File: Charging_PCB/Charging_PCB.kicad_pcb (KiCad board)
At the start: 2 copper layers, 8 parts, among them K3 BMS_Relay, K4 IMD_Relay, Q1 PMOS, Q2 PMOS

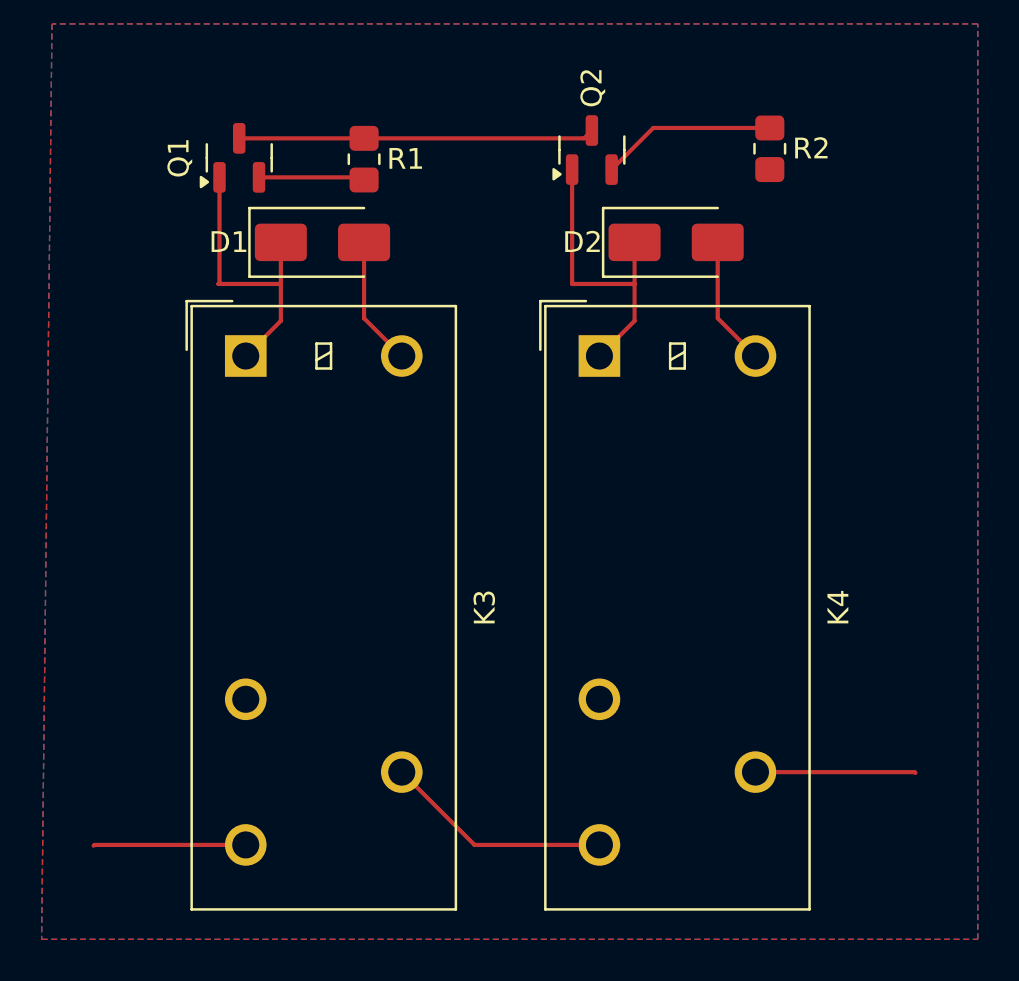
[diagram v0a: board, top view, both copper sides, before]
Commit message: unfinished connector addition to schematic
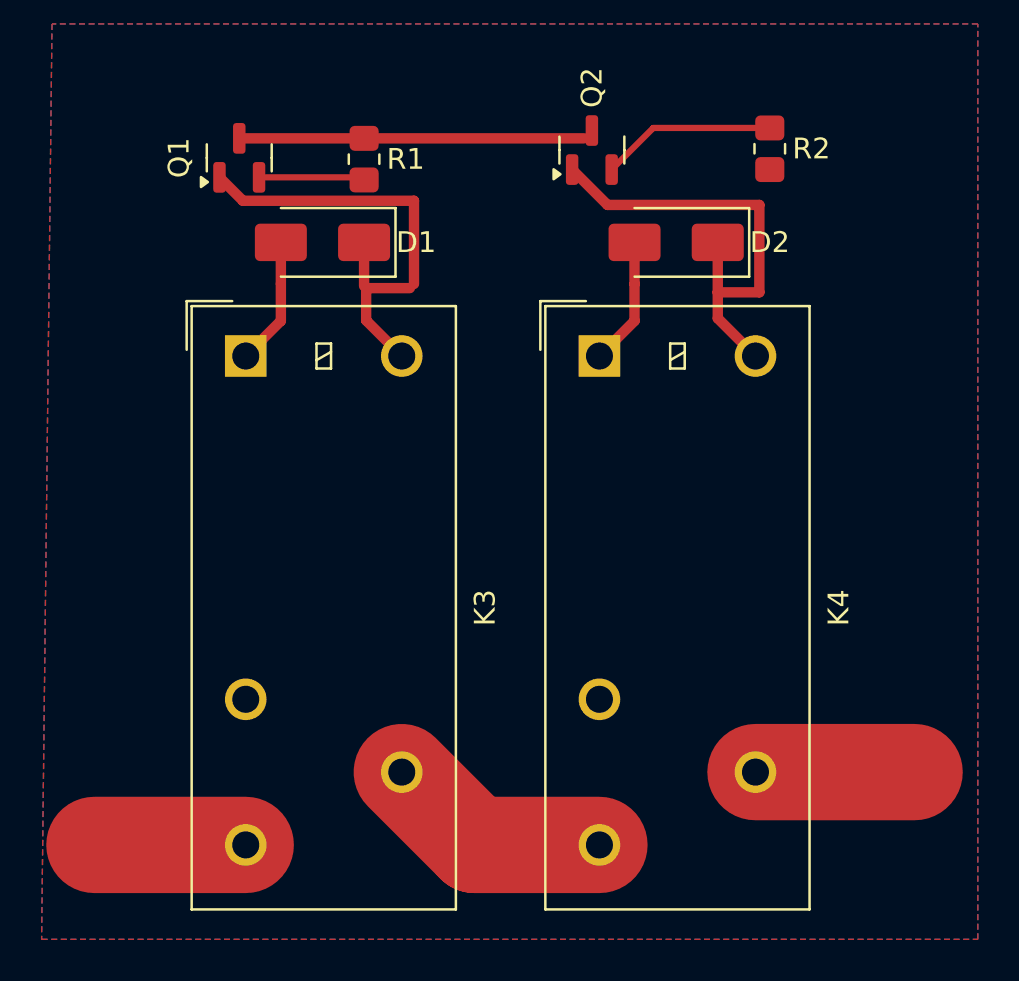
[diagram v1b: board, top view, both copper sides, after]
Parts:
- turned D1 to 180 degrees
- turned D2 to 180 degrees
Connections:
- D1 pad 2: GND -> /+12_Relay
- D2 pad 2: GND -> /+12_Relay
- K3 pad 11: Net-(K3-Pad11) -> /+12_Relay
- K3 pad A1: GND -> /+12_Relay
- K4 pad 11: Net-(K4-Pad11) -> /+12_Relay
- K4 pad 14: Net-(K3-Pad11) -> /+12_Relay
- K4 pad A1: GND -> /+12_Relay
- R2 pad 2: GND -> Net-(K3-Pad11)
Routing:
- net /+12_Relay: track 7.33 -> 38.3 mm
- net GND: track 12.4 -> 0.00 mm
- net Net-(K3-Pad11): track 10.9 -> 0.00 mm
- net Net-(D1-K): track 14.3 -> 22.4 mm
- net Net-(K4-Pad11): track 7.70 -> 0.00 mm
- net Net-(D2-K): track 14.7 -> 22.1 mm

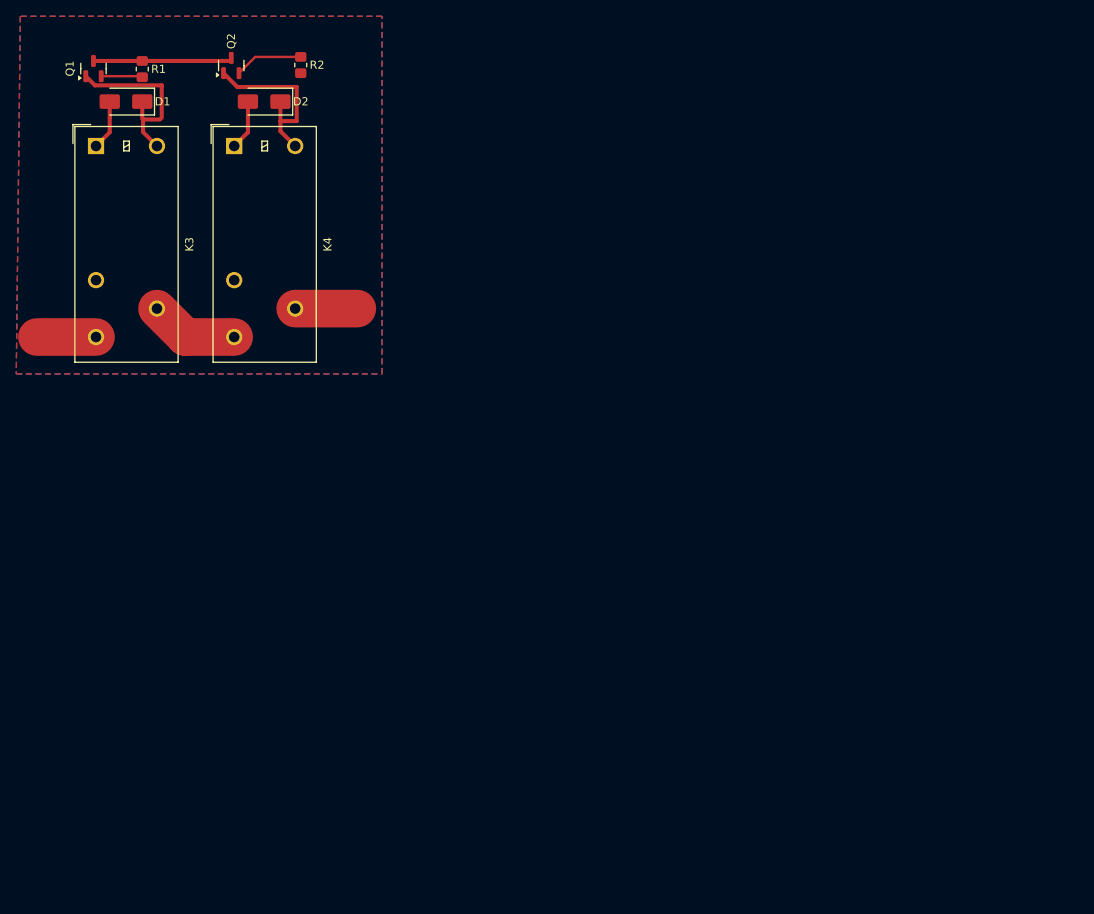
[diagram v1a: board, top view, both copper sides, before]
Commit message: added connectors, relay traces, mounting holes, labels
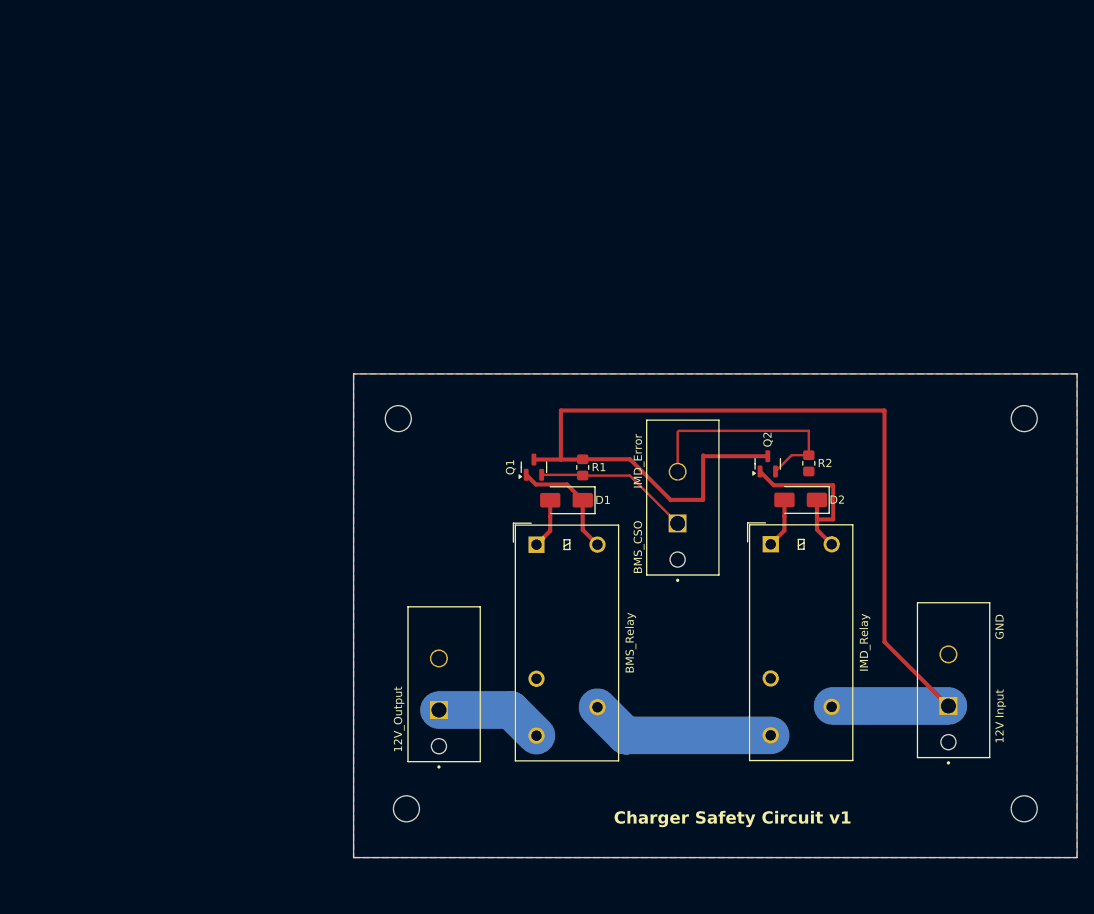
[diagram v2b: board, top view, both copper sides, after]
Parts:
- added 12V Input              GND: 12V Input, 641964-1:TE_641964-1, F.Cu at (179.7, 114.8)
- added 12V_Output: Relay Output, 641964-1:TE_641964-1, F.Cu at (117.0, 115.3)
- added BMS_CSO         IMD_Error: Signal Inputs, 641964-1:TE_641964-1, F.Cu at (146.4, 92.4)
- added H101: MountingHole, MountingHole:MountingHole_3.2mm_M3, F.Cu at (189.0, 79.5)
- added H102: MountingHole, MountingHole:MountingHole_3.2mm_M3, F.Cu at (112.0, 79.5)
- added H103: MountingHole, MountingHole:MountingHole_3.2mm_M3, F.Cu at (189.0, 127.5)
- added H104: MountingHole, MountingHole:MountingHole_3.2mm_M3, F.Cu at (113.0, 127.5)
- moved D2 82.2 mm to (161.5, 89.5)
- moved IMD_Relay 82.2 mm to (157.8, 95.0)
- moved Q2 82.2 mm to (157.4, 85.1)
- moved R2 79.4 mm to (162.5, 85.0)
- moved BMS_Relay 73.1 mm to (129.0, 95.0)
- moved D1 73.1 mm to (132.7, 89.5)
- moved Q1 73.1 mm to (128.7, 85.5)
- moved R1 73.1 mm to (134.7, 85.5)
- renumbered K3 to BMS_Relay, K4 to IMD_Relay
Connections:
- net /CSO renamed /BMS_CSO
- net /IMD_error renamed /IMD_Error
- BMS_Relay pad 11: /+12_Relay -> Net-(K3-Pad11)
- BMS_Relay pad A1: /+12_Relay -> GND
- D1 pad 2: /+12_Relay -> GND
- D2 pad 2: /+12_Relay -> GND
- IMD_Relay pad 11: /+12_Relay -> +12V
- IMD_Relay pad 14: /+12_Relay -> Net-(K3-Pad11)
- IMD_Relay pad A1: /+12_Relay -> GND
- R2 pad 2: Net-(K3-Pad11) -> GND
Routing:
- net +12V: track 17.1 -> 136.3 mm
- net /+12_Relay: track 38.3 -> 13.3 mm
- net Net-(K3-Pad11): track 0.00 -> 22.8 mm
- net /IMD_Error: track 8.43 -> 29.0 mm
- net /BMS_CSO: track 5.10 -> 19.2 mm
- net GND: track 0.00 -> 12.3 mm
- net Net-(D1-K): track 22.4 -> 14.5 mm
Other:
- board outline added: 89 x 59.5 mm
- board text added: "Charger Safety Circuit v1"

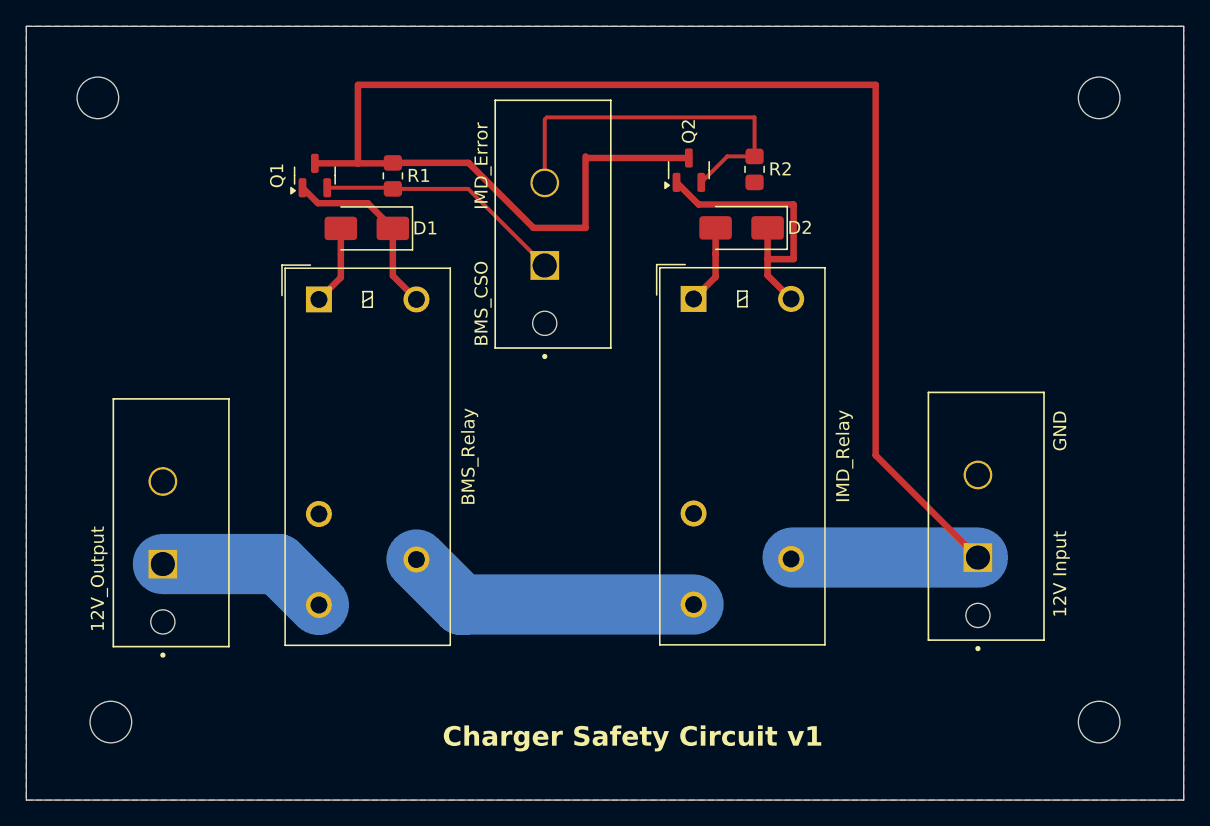
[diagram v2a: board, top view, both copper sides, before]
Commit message: Fillet edges, shrunk relay traces, fixed labels for vinh
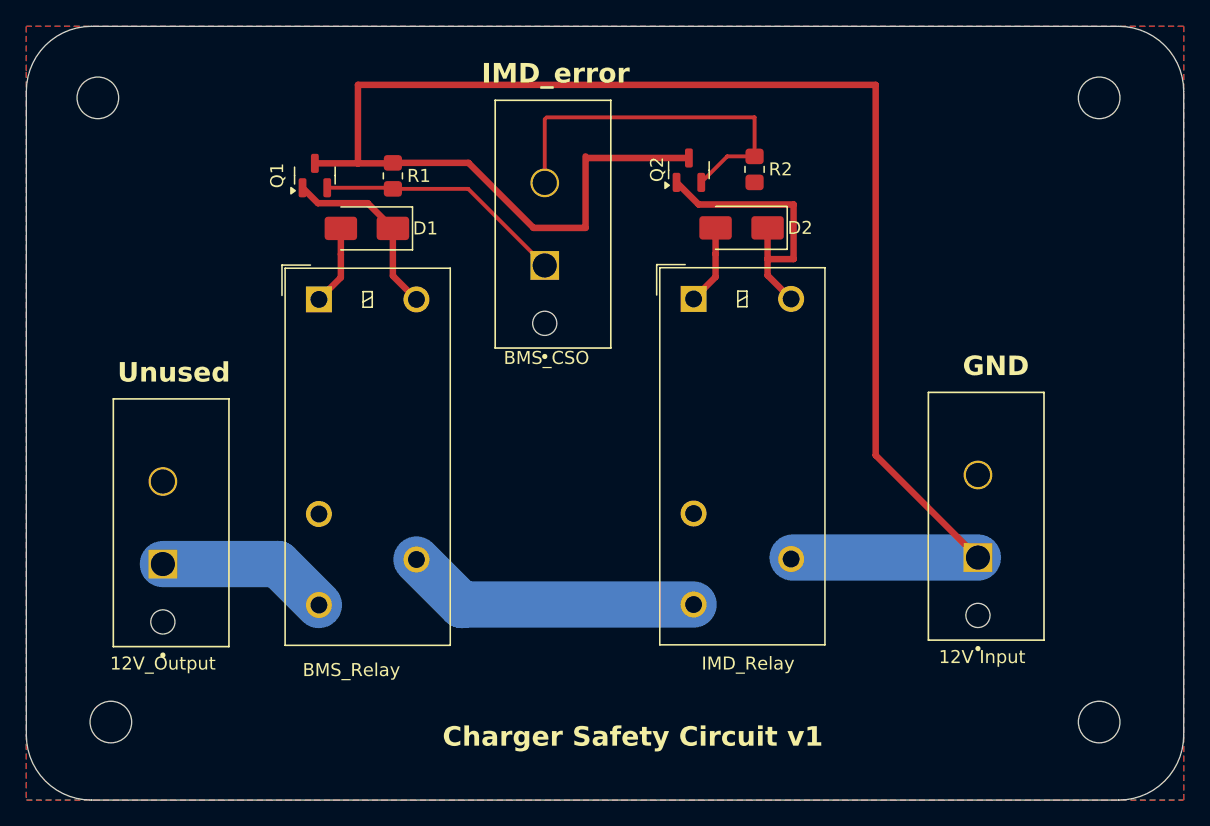
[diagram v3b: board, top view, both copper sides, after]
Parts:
- 12V Input: renamed from 12V Input              GND
- BMS_CSO: renamed from BMS_CSO         IMD_Error
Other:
- outline, holes or cut-outs redrawn
- board text added: "GND"
- board text added: "IMD_error"
- board text added: "Unused"
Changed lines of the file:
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@@
 		(at 117 115.35 90)
 		(property "Reference" "12V_Output"
-			(at -1.15 -5 270)
+			(at -7.65 0 0)
 			(layer "F.SilkS")
 			(effects
@@
 		(tags "Omron Relay SPDT")
 		(property "Reference" "IMD_Relay"
-			(at 11.5 12.1 90)
+			(at 4.1875 28.0375 180)
 			(layer "F.SilkS")
 			(effects
@@
 		(tags "Omron Relay SPDT")
 		(property "Reference" "BMS_Relay"
-			(at 11.5 12.1 90)
+			(at 2.5 28.5 180)
 			(layer "F.SilkS")
 			(effects
@@
 		(layer "F.Cu")
 		(at 179.6775 114.85 90)
-		(property "Reference" "12V Input              GND"
-			(at 3.35 6.3225 90)
+		(property "Reference" "12V Input"
+			(at -7.65 0.3225 180)
 			(layer "F.SilkS")
 			(effects
@@
 		(tags "SOT TO_SOT_SMD")
 		(property "Reference" "Q2"
-			(at 3 0 90)
+			(at 0.0625 -2.45 90)
 			(layer "F.SilkS")
 			(effects
@@
 		)
 		(property "Value" "PMOS"
-			(at 0 2.4 90)
+			(at 2.5625 -0.95 180)
 			(layer "F.Fab")
 			(effects
@@
 		(layer "F.Cu")
 		(at 146.365 92.3875 90)
-		(property "Reference" "BMS_CSO         IMD_Error"
-			(at 2.3875 -4.865 90)
+		(property "Reference" "BMS_CSO"
+			(at -7.1125 0.135 180)
 			(layer "F.SilkS")
 			(effects
@@
 		(embedded_fonts no)
 	)
-	(gr_poly
-		(pts
-			(xy 106.5 74) (xy 106.5 133.5) (xy 195.5 133.5) (xy 195.5 74)
+	(gr_line
+		(start 111.5 133.5)
+		(end 190.5 133.5)
+		(stroke
+			(width 0.05)
+			(type default)
+		)
+		(layer "Edge.Cuts")
+	)
+	(gr_arc
+		(start 190.5 74)
+		(mid 194.035534 75.464466)
+		(end 195.5 79)
+		(stroke
+			(width 0.05)
+			(type default)
+		)
+		(layer "Edge.Cuts")
+	)
+	(gr_line
+		(start 106.5 79)
+		(end 106.5 128.5)
+		(stroke
+			(width 0.05)
+			(type default)
+		)
+		(layer "Edge.Cuts")
+	)
+	(gr_arc
+		(start 195.5 128.5)
+		(mid 194.035534 132.035534)
+		(end 190.5 133.5)
+		(stroke
+			(width 0.05)
+			(type default)
+		)
+		(layer "Edge.Cuts")
+	)
+	(gr_arc
+		(start 111.5 133.5)
+		(mid 107.964466 132.035534)
+		(end 106.5 128.5)
+		(stroke
+			(width 0.05)
+			(type default)
+		)
+		(layer "Edge.Cuts")
+	)
+	(gr_line
+		(start 190.5 74)
+		(end 111.5 74)
+		(stroke
+			(width 0.05)
+			(type default)
+		)
+		(layer "Edge.Cuts")
+	)
+	(gr_arc
+		(start 106.5 79)
+		(mid 107.964466 75.464466)
+		(end 111.5 74)
+		(stroke
+			(width 0.05)
+			(type default)
 		)
+		(layer "Edge.Cuts")
+	)
+	(gr_line
+		(start 195.5 128.5)
+		(end 195.5 79)
 		(stroke
 			(width 0.05)
-			(type solid)
+			(type default)
 		)
-		(fill no)
 		(layer "Edge.Cuts")
 	)
+	(gr_text "GND"
+		(at 178.5 101 0)
+		(layer "F.SilkS")
+		(effects
+			(font
+				(size 1.5 1.5)
+				(thickness 0.3)
+				(bold yes)
+			)
+			(justify left bottom)
+		)
+	)
+	(gr_text "Unused"
+		(at 113.5 101.5 0)
+		(layer "F.SilkS")
+		(effects
+			(font
+				(size 1.5 1.5)
+				(thickness 0.3)
+				(bold yes)
+			)
+			(justify left bottom)
+		)
+	)
+	(gr_text "IMD_error"
+		(at 141.5 78.5 0)
+		(layer "F.SilkS")
+		(effects
+			(font
+				(size 1.5 1.5)
+				(thickness 0.3)
+				(bold yes)
+			)
+			(justify left bottom)
+		)
+	)
 	(gr_text "Charger Safety Circuit v1 "
 		(at 138.5 129.5 0)
@@
 		(start 157.8125 118.4625)
 		(end 140.0375 118.4625)
-		(width 4.63)
+		(width 3.56)
 		(layer "B.Cu")
 		(net 5)
@@
 		(start 140 118.5)
 		(end 136.5 115)
-		(width 4.63)
+		(width 3.56)
 		(layer "B.Cu")
 		(net 5)
@@
 		(start 140.0375 118.4625)
 		(end 140 118.5)
-		(width 4.63)
+		(width 3.56)
 		(layer "B.Cu")
 		(net 5)
@@
 		(start 117 115.35)
 		(end 125.85 115.35)
-		(width 4.63)
+		(width 3.56)
 		(layer "B.Cu")
 		(net 6)
@@
 		(start 125.85 115.35)
 		(end 129 118.5)
-		(width 4.63)
+		(width 3.56)
 		(layer "B.Cu")
 		(net 6)
@@
 		(start 179.6775 114.85)
 		(end 165.425 114.85)
-		(width 4.63)
+		(width 3.56)
 		(layer "B.Cu")
 		(net 8)

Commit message: Finished all part#'s. generated gerber and BOM files
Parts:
- Q1, Q2: footprint Package_TO_SOT_SMD:SOT-23 -> Package_TO_SOT_SMD:SOT-523
- U112: renamed from 12V Input; value 12V Input -> Charger Input
- renumbered BMS_Relay to K3, IMD_Relay to K4, BMS_CSO to U113, 12V_Output to U114
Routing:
- net /BMS_CSO: track 19.2 -> 19.8 mm
